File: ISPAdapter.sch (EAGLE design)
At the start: 9 parts, among them U1 SWITCH_IC_QUAD74LVC4066

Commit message: TSSOP
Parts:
- U1: value SWITCH_IC_QUAD74LVC4066 -> 74LVC4066PW; device dubec:SWITCH_IC_QUAD74LVC4066 -> dubec:74LVC4066PW
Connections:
- removed net MISO_A: J1.1, U1.2A
- removed net MOSI_A: J1.4, U1.4A
- removed net SCK_A: J1.3, U1.1A
- new net MISO_PROG: J1.1, U1.3Y
- new net MOSI_PROG: J1.4, U1.2Y
- new net SCK_PROG: J1.3, U1.4Y
- net DGND: now also U1.1E, U1.1Y, U1.1Z; no longer U1.3A, U1.3B, U1.3C
- net ISP_EN: now also U1.2E, U1.3E, U1.4E; no longer U1.1C, U1.2C, U1.4C
- net MISO: now also U1.3Z; no longer U1.2B
- net MOSI: now also U1.2Z; no longer U1.4B
- net SCK: now also U1.4Z; no longer U1.1B
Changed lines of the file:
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@@
 <part name="GND1" library="SparkFun-Aesthetics" deviceset="GND" device=""/>
 <part name="JP3" library="SparkFun-Connectors" deviceset="M01" device="PTH"/>
-<part name="U1" library="dubec" deviceset="SWITCH_IC_QUAD" device="74LVC4066" value="SWITCH_IC_QUAD74LVC4066"/>
+<part name="U1" library="dubec" deviceset="74LVC4066" device="PW" value="74LVC4066PW"/>
 <part name="S1" library="SparkFun-Electromechanical" deviceset="SWITCH-SPDT" device="ESWITCH"/>
 <part name="GND6" library="SparkFun-Aesthetics" deviceset="GND" device=""/>
@@
 </segment>
 <segment>
-<pinref part="U1" gate="G$1" pin="4B"/>
-<wire x1="71.12" y1="45.72" x2="73.66" y2="45.72" width="0.1524" layer="91"/>
-<label x="73.66" y="45.72" size="1.27" layer="95" xref="yes"/>
+<pinref part="U1" gate="G$1" pin="2Z"/>
+<wire x1="45.72" y1="50.8" x2="43.18" y2="50.8" width="0.1524" layer="91"/>
+<label x="43.18" y="50.8" size="1.27" layer="95" rot="R180" xref="yes"/>
 </segment>
 </net>
@@
 </segment>
 <segment>
-<pinref part="U1" gate="G$1" pin="GND"/>
-<wire x1="45.72" y1="40.64" x2="43.18" y2="40.64" width="0.1524" layer="91"/>
-<pinref part="U1" gate="G$1" pin="3C"/>
-<wire x1="45.72" y1="43.18" x2="43.18" y2="43.18" width="0.1524" layer="91"/>
-<wire x1="43.18" y1="43.18" x2="43.18" y2="40.64" width="0.1524" layer="91"/>
-</segment>
-<segment>
 <pinref part="GND6" gate="1" pin="GND"/>
 <wire x1="43.18" y1="40.64" x2="43.18" y2="33.02" width="0.1524" layer="91"/>
 <wire x1="86.36" y1="33.02" x2="86.36" y2="30.48" width="0.1524" layer="91"/>
-<wire x1="43.18" y1="33.02" x2="73.66" y2="33.02" width="0.1524" layer="91"/>
+<wire x1="43.18" y1="33.02" x2="86.36" y2="33.02" width="0.1524" layer="91"/>
 <junction x="86.36" y="33.02"/>
 <pinref part="C1" gate="G$1" pin="2"/>
-<wire x1="73.66" y1="33.02" x2="86.36" y2="33.02" width="0.1524" layer="91"/>
 <wire x1="83.82" y1="60.96" x2="86.36" y2="60.96" width="0.1524" layer="91"/>
 <wire x1="86.36" y1="60.96" x2="86.36" y2="33.02" width="0.1524" layer="91"/>
-<pinref part="U1" gate="G$1" pin="3B"/>
-<wire x1="71.12" y1="43.18" x2="73.66" y2="43.18" width="0.1524" layer="91"/>
-<pinref part="U1" gate="G$1" pin="3A"/>
-<wire x1="71.12" y1="40.64" x2="73.66" y2="40.64" width="0.1524" layer="91"/>
-<wire x1="73.66" y1="43.18" x2="73.66" y2="40.64" width="0.1524" layer="91"/>
-<wire x1="73.66" y1="40.64" x2="73.66" y2="33.02" width="0.1524" layer="91"/>
-<junction x="73.66" y="40.64"/>
-<junction x="73.66" y="33.02"/>
+<pinref part="U1" gate="G$1" pin="GND"/>
+<wire x1="45.72" y1="40.64" x2="43.18" y2="40.64" width="0.1524" layer="91"/>
 </segment>
 <segment>
@@
 <pinref part="C2" gate="G$1" pin="2"/>
 </segment>
+<segment>
+<pinref part="U1" gate="G$1" pin="1Z"/>
+<wire x1="45.72" y1="53.34" x2="43.18" y2="53.34" width="0.1524" layer="91"/>
+<pinref part="U1" gate="G$1" pin="1Y"/>
+<wire x1="45.72" y1="55.88" x2="43.18" y2="55.88" width="0.1524" layer="91"/>
+<wire x1="43.18" y1="53.34" x2="43.18" y2="55.88" width="0.1524" layer="91"/>
+<wire x1="43.18" y1="55.88" x2="40.64" y2="55.88" width="0.1524" layer="91"/>
+<junction x="43.18" y="55.88"/>
+<label x="40.64" y="55.88" size="1.27" layer="95" rot="R180" xref="yes"/>
+</segment>
+<segment>
+<pinref part="U1" gate="G$1" pin="1E"/>
+<wire x1="71.12" y1="53.34" x2="73.66" y2="53.34" width="0.1524" layer="91"/>
+<label x="73.66" y="53.34" size="1.27" layer="95" xref="yes"/>
+</segment>
 </net>
 <net name="MISO" class="0">
@@
 </segment>
 <segment>
-<pinref part="U1" gate="G$1" pin="2B"/>
-<wire x1="45.72" y1="50.8" x2="43.18" y2="50.8" width="0.1524" layer="91"/>
-<label x="43.18" y="50.8" size="1.27" layer="95" rot="R180" xref="yes"/>
+<pinref part="U1" gate="G$1" pin="3Z"/>
+<wire x1="71.12" y1="43.18" x2="73.66" y2="43.18" width="0.1524" layer="91"/>
+<label x="73.66" y="43.18" size="1.27" layer="95" xref="yes"/>
 </segment>
 </net>
@@
 </segment>
 <segment>
-<pinref part="U1" gate="G$1" pin="1B"/>
-<wire x1="45.72" y1="53.34" x2="43.18" y2="53.34" width="0.1524" layer="91"/>
-<label x="43.18" y="53.34" size="1.27" layer="95" rot="R180" xref="yes"/>
+<pinref part="U1" gate="G$1" pin="4Z"/>
+<wire x1="71.12" y1="45.72" x2="73.66" y2="45.72" width="0.1524" layer="91"/>
+<label x="73.66" y="45.72" size="1.27" layer="95" xref="yes"/>
 </segment>
 </net>
@@
 <net name="ISP_EN" class="0">
 <segment>
-<pinref part="U1" gate="G$1" pin="1C"/>
-<wire x1="71.12" y1="53.34" x2="73.66" y2="53.34" width="0.1524" layer="91"/>
-<label x="73.66" y="53.34" size="1.27" layer="95" xref="yes"/>
-</segment>
-<segment>
-<pinref part="U1" gate="G$1" pin="2C"/>
+<pinref part="U1" gate="G$1" pin="2E"/>
 <wire x1="45.72" y1="45.72" x2="43.18" y2="45.72" width="0.1524" layer="91"/>
 <label x="43.18" y="45.72" size="1.27" layer="95" rot="R180" xref="yes"/>
@@
 </segment>
 <segment>
-<pinref part="U1" gate="G$1" pin="4C"/>
+<pinref part="U1" gate="G$1" pin="4E"/>
 <wire x1="71.12" y1="50.8" x2="73.66" y2="50.8" width="0.1524" layer="91"/>
 <label x="73.66" y="50.8" size="1.27" layer="95" xref="yes"/>
 </segment>
-</net>
-<net name="SCK_A" class="0">
+<segment>
+<pinref part="U1" gate="G$1" pin="3E"/>
+<wire x1="45.72" y1="43.18" x2="43.18" y2="43.18" width="0.1524" layer="91"/>
+<label x="43.18" y="43.18" size="1.27" layer="95" rot="R180" xref="yes"/>
+</segment>
+</net>
+<net name="SCK_PROG" class="0">
 <segment>
 <pinref part="J1" gate="G$1" pin="3"/>
@@
 </segment>
 <segment>
-<pinref part="U1" gate="G$1" pin="1A"/>
-<wire x1="45.72" y1="55.88" x2="43.18" y2="55.88" width="0.1524" layer="91"/>
-<label x="43.18" y="55.88" size="1.27" layer="95" rot="R180" xref="yes"/>
-</segment>
-</net>
-<net name="MISO_A" class="0">
+<pinref part="U1" gate="G$1" pin="4Y"/>
+<wire x1="71.12" y1="48.26" x2="73.66" y2="48.26" width="0.1524" layer="91"/>
+<label x="73.66" y="48.26" size="1.27" layer="95" xref="yes"/>
+</segment>
+</net>
+<net name="MISO_PROG" class="0">
 <segment>
 <pinref part="J1" gate="G$1" pin="1"/>
@@
 </segment>
 <segment>
-<pinref part="U1" gate="G$1" pin="2A"/>
-<wire x1="45.72" y1="48.26" x2="43.18" y2="48.26" width="0.1524" layer="91"/>
-<label x="43.18" y="48.26" size="1.27" layer="95" rot="R180" xref="yes"/>
-</segment>
-</net>
-<net name="MOSI_A" class="0">
+<pinref part="U1" gate="G$1" pin="3Y"/>
+<wire x1="71.12" y1="40.64" x2="73.66" y2="40.64" width="0.1524" layer="91"/>
+<label x="73.66" y="40.64" size="1.27" layer="95" xref="yes"/>
+</segment>
+</net>
+<net name="MOSI_PROG" class="0">
 <segment>
 <pinref part="J1" gate="G$1" pin="4"/>
@@
 </segment>
 <segment>
-<pinref part="U1" gate="G$1" pin="4A"/>
-<wire x1="71.12" y1="48.26" x2="73.66" y2="48.26" width="0.1524" layer="91"/>
-<label x="73.66" y="48.26" size="1.27" layer="95" xref="yes"/>
-</segment>
-</net>
+<pinref part="U1" gate="G$1" pin="2Y"/>
+<wire x1="45.72" y1="48.26" x2="43.18" y2="48.26" width="0.1524" layer="91"/>
+<label x="43.18" y="48.26" size="1.27" layer="95" rot="R180" xref="yes"/>
+</segment>
+</net>

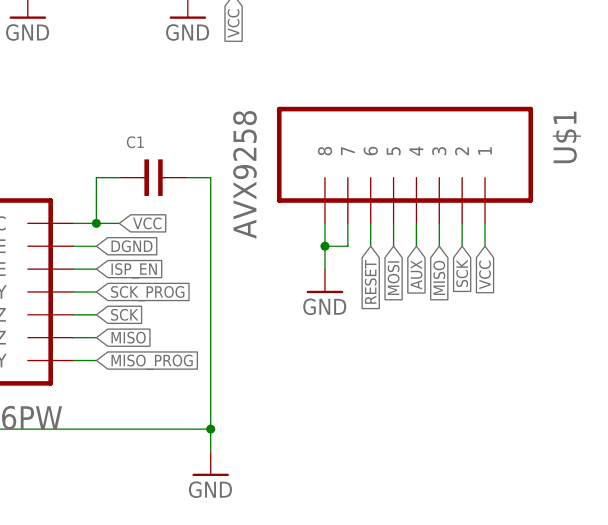
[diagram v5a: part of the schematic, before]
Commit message: Layout updates, land pattern tweaks
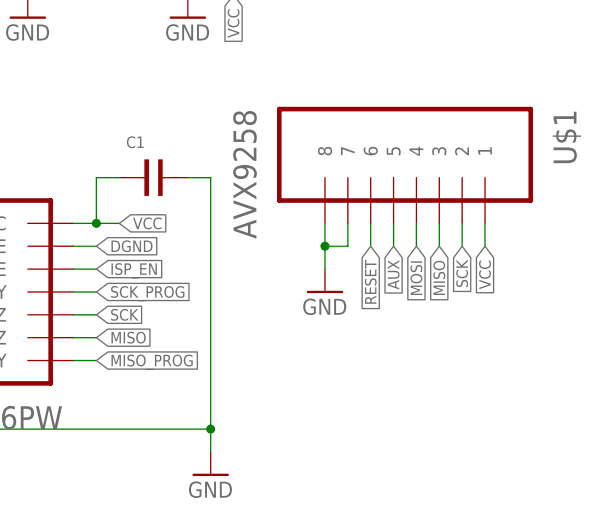
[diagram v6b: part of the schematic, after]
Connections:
- net AUX: now also U$1.5; no longer U$1.4
- net MOSI: now also U$1.4; no longer U$1.5
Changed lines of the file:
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@@
 <net name="MOSI" class="0">
-<segment>
-<pinref part="U$1" gate="G$1" pin="5"/>
-<wire x1="106.68" y1="55.88" x2="106.68" y2="53.34" width="0.1524" layer="91"/>
-<label x="106.68" y="53.34" size="1.27" layer="95" rot="R270" xref="yes"/>
-</segment>
 <segment>
 <pinref part="U1" gate="G$1" pin="2Z"/>
 <wire x1="45.72" y1="50.8" x2="43.18" y2="50.8" width="0.1524" layer="91"/>
 <label x="43.18" y="50.8" size="1.27" layer="95" rot="R180" xref="yes"/>
+</segment>
+<segment>
+<pinref part="U$1" gate="G$1" pin="4"/>
+<wire x1="109.22" y1="55.88" x2="109.22" y2="53.34" width="0.1524" layer="91"/>
+<label x="109.22" y="53.34" size="1.27" layer="95" rot="R270" xref="yes"/>
 </segment>
 </net>
@@
 <net name="AUX" class="0">
 <segment>
-<pinref part="U$1" gate="G$1" pin="4"/>
-<wire x1="109.22" y1="55.88" x2="109.22" y2="53.34" width="0.1524" layer="91"/>
-<label x="109.22" y="53.34" size="1.27" layer="95" rot="R270" xref="yes"/>
-</segment>
-<segment>
 <pinref part="JP3" gate="G$1" pin="1"/>
 <wire x1="45.72" y1="83.82" x2="45.72" y2="81.28" width="0.1524" layer="91"/>
 <label x="45.72" y="81.28" size="1.27" layer="95" rot="R270" xref="yes"/>
 </segment>
+<segment>
+<pinref part="U$1" gate="G$1" pin="5"/>
+<wire x1="106.68" y1="55.88" x2="106.68" y2="53.34" width="0.1524" layer="91"/>
+<label x="106.68" y="53.34" size="1.27" layer="95" rot="R270" xref="yes"/>
+</segment>
 </net>

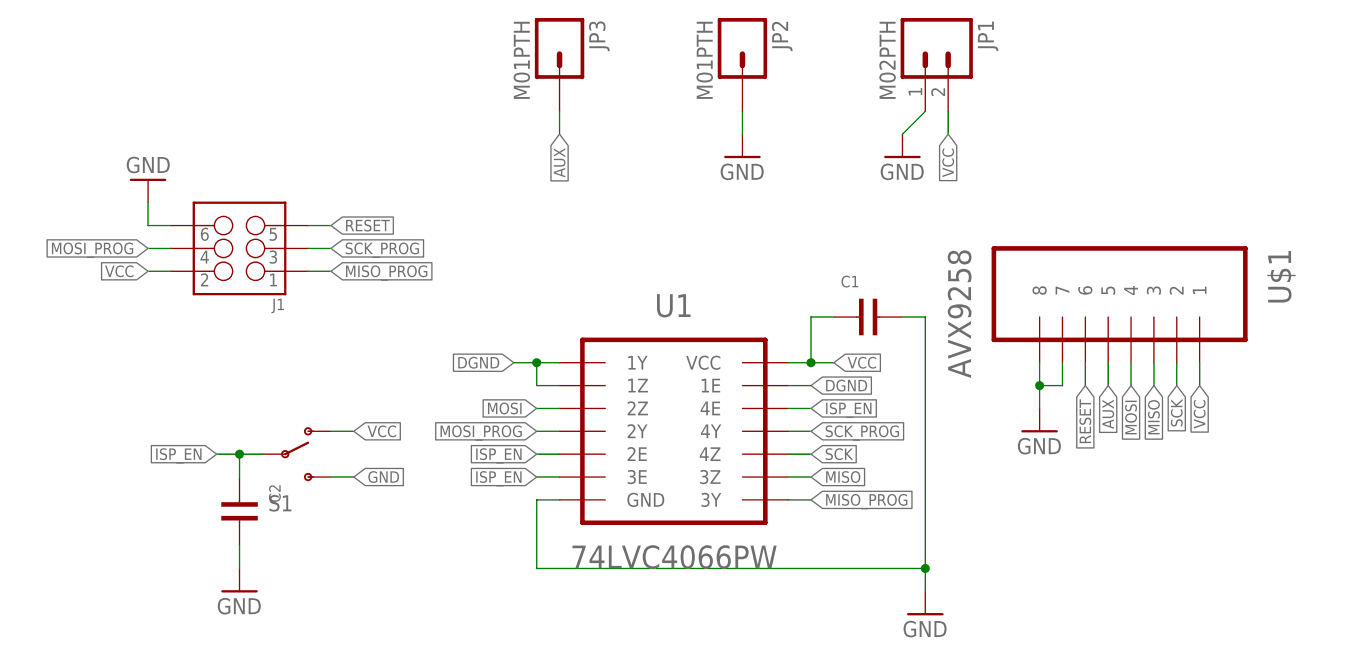
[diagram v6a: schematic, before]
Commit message: Jack/Plug refs; offset pads
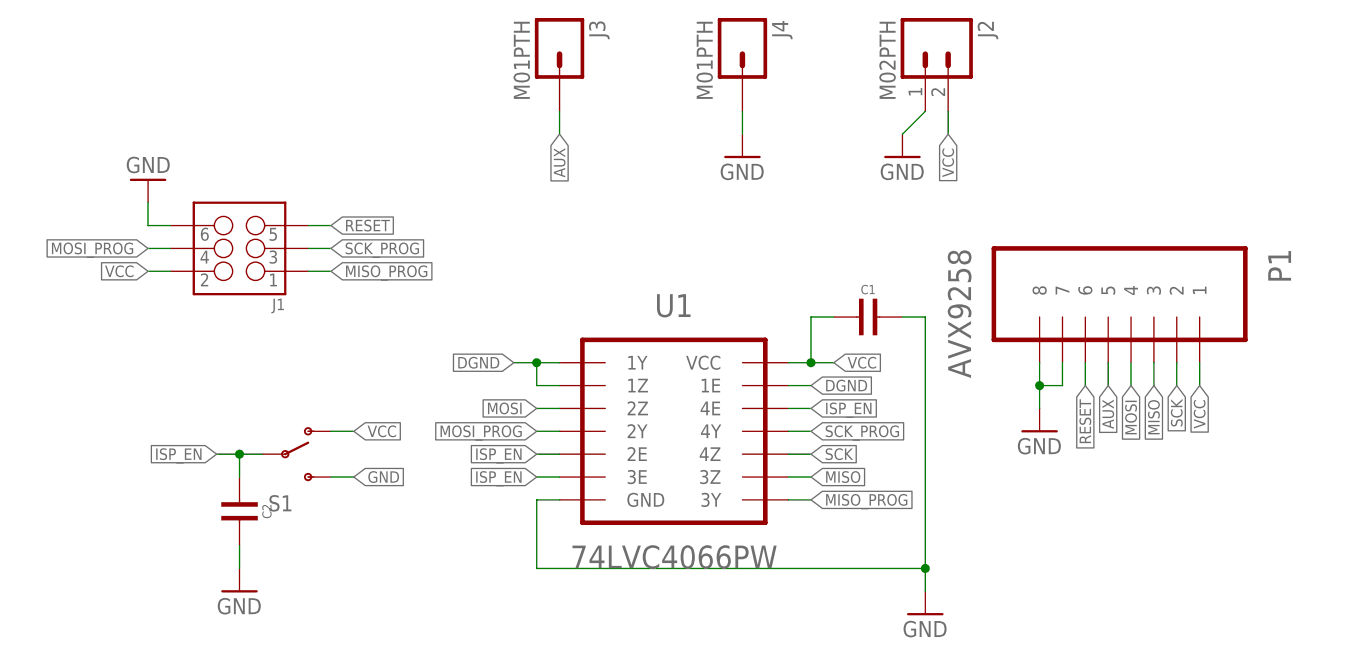
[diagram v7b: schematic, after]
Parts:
- renumbered JP1 to J2, JP2 to J4, JP3 to J3, U$1 to P1
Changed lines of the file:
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@@
 <part name="GND2" library="SparkFun-Aesthetics" deviceset="GND" device=""/>
 <part name="J1" library="SparkFun-Connectors" deviceset="M03X2" device="WR"/>
-<part name="JP1" library="SparkFun-Connectors" deviceset="M02" device="PTH"/>
+<part name="J2" library="SparkFun-Connectors" deviceset="M02" device="PTH"/>
 <part name="GND3" library="SparkFun-Aesthetics" deviceset="GND" device=""/>
-<part name="U$1" library="dubec" deviceset="AVX9258" device=""/>
+<part name="P1" library="dubec" deviceset="AVX9258" device=""/>
 <part name="GND4" library="SparkFun-Aesthetics" deviceset="GND" device=""/>
-<part name="JP2" library="SparkFun-Connectors" deviceset="M01" device="PTH"/>
+<part name="J4" library="SparkFun-Connectors" deviceset="M01" device="PTH"/>
 <part name="GND1" library="SparkFun-Aesthetics" deviceset="GND" device=""/>
-<part name="JP3" library="SparkFun-Connectors" deviceset="M01" device="PTH"/>
+<part name="J3" library="SparkFun-Connectors" deviceset="M01" device="PTH"/>
 <part name="U1" library="dubec" deviceset="74LVC4066" device="PW" value="74LVC4066PW"/>
 <part name="S1" library="SparkFun-Electromechanical" deviceset="SWITCH-SPDT" device="ESWITCH"/>
@@
 <instance part="GND2" gate="1" x="0" y="76.2" rot="R180"/>
 <instance part="J1" gate="G$1" x="10.16" y="68.58" rot="R180"/>
-<instance part="JP1" gate="G$1" x="86.36" y="91.44" rot="R270"/>
+<instance part="J2" gate="G$1" x="86.36" y="91.44" rot="R270"/>
 <instance part="GND3" gate="1" x="83.82" y="78.74"/>
-<instance part="U$1" gate="G$1" x="109.22" y="63.5" rot="R270"/>
+<instance part="P1" gate="G$1" x="109.22" y="63.5" rot="R270"/>
 <instance part="GND4" gate="1" x="99.06" y="48.26"/>
-<instance part="JP2" gate="G$1" x="66.04" y="91.44" rot="R270"/>
+<instance part="J4" gate="G$1" x="66.04" y="91.44" rot="R270"/>
 <instance part="GND1" gate="1" x="66.04" y="78.74"/>
-<instance part="JP3" gate="G$1" x="45.72" y="91.44" rot="R270"/>
+<instance part="J3" gate="G$1" x="45.72" y="91.44" rot="R270"/>
 <instance part="U1" gate="G$1" x="58.42" y="48.26"/>
 <instance part="S1" gate="1" x="15.24" y="45.72"/>
@@
 </segment>
 <segment>
-<pinref part="JP1" gate="G$1" pin="2"/>
+<pinref part="J2" gate="G$1" pin="2"/>
 <wire x1="88.9" y1="83.82" x2="88.9" y2="81.28" width="0.1524" layer="91"/>
 <label x="88.9" y="81.28" size="1.27" layer="95" rot="R270" xref="yes"/>
 </segment>
 <segment>
-<pinref part="U$1" gate="G$1" pin="1"/>
+<pinref part="P1" gate="G$1" pin="1"/>
 <wire x1="116.84" y1="55.88" x2="116.84" y2="53.34" width="0.1524" layer="91"/>
 <label x="116.84" y="53.34" size="1.27" layer="95" rot="R270" xref="yes"/>
@@
 </segment>
 <segment>
-<pinref part="U$1" gate="G$1" pin="4"/>
+<pinref part="P1" gate="G$1" pin="4"/>
 <wire x1="109.22" y1="55.88" x2="109.22" y2="53.34" width="0.1524" layer="91"/>
 <label x="109.22" y="53.34" size="1.27" layer="95" rot="R270" xref="yes"/>
@@
 </segment>
 <segment>
-<pinref part="JP1" gate="G$1" pin="1"/>
+<pinref part="J2" gate="G$1" pin="1"/>
 <wire x1="86.36" y1="83.82" x2="83.82" y2="81.28" width="0.1524" layer="91"/>
 <pinref part="GND3" gate="1" pin="GND"/>
@@
 <segment>
 <pinref part="GND4" gate="1" pin="GND"/>
-<pinref part="U$1" gate="G$1" pin="7"/>
-<pinref part="U$1" gate="G$1" pin="8"/>
+<pinref part="P1" gate="G$1" pin="7"/>
+<pinref part="P1" gate="G$1" pin="8"/>
 <wire x1="99.06" y1="55.88" x2="99.06" y2="53.34" width="0.1524" layer="91"/>
 <wire x1="99.06" y1="53.34" x2="99.06" y2="50.8" width="0.1524" layer="91"/>
@@
 <net name="MISO" class="0">
 <segment>
-<pinref part="U$1" gate="G$1" pin="3"/>
+<pinref part="P1" gate="G$1" pin="3"/>
 <wire x1="111.76" y1="55.88" x2="111.76" y2="53.34" width="0.1524" layer="91"/>
 <label x="111.76" y="53.34" size="1.27" layer="95" rot="R270" xref="yes"/>
@@
 <net name="SCK" class="0">
 <segment>
-<pinref part="U$1" gate="G$1" pin="2"/>
+<pinref part="P1" gate="G$1" pin="2"/>
 <wire x1="114.3" y1="55.88" x2="114.3" y2="53.34" width="0.1524" layer="91"/>
 <label x="114.3" y="53.34" size="1.27" layer="95" rot="R270" xref="yes"/>
@@
 </segment>
 <segment>
-<pinref part="U$1" gate="G$1" pin="6"/>
+<pinref part="P1" gate="G$1" pin="6"/>
 <wire x1="104.14" y1="55.88" x2="104.14" y2="53.34" width="0.1524" layer="91"/>
 <label x="104.14" y="53.34" size="1.27" layer="95" rot="R270" xref="yes"/>
@@
 <net name="GND" class="0">
 <segment>
-<pinref part="JP2" gate="G$1" pin="1"/>
+<pinref part="J4" gate="G$1" pin="1"/>
 <wire x1="66.04" y1="83.82" x2="66.04" y2="81.28" width="0.1524" layer="91"/>
 <pinref part="GND1" gate="1" pin="GND"/>
@@
 <net name="AUX" class="0">
 <segment>
-<pinref part="JP3" gate="G$1" pin="1"/>
+<pinref part="J3" gate="G$1" pin="1"/>
 <wire x1="45.72" y1="83.82" x2="45.72" y2="81.28" width="0.1524" layer="91"/>
 <label x="45.72" y="81.28" size="1.27" layer="95" rot="R270" xref="yes"/>
 </segment>
 <segment>
-<pinref part="U$1" gate="G$1" pin="5"/>
+<pinref part="P1" gate="G$1" pin="5"/>
 <wire x1="106.68" y1="55.88" x2="106.68" y2="53.34" width="0.1524" layer="91"/>
 <label x="106.68" y="53.34" size="1.27" layer="95" rot="R270" xref="yes"/>
